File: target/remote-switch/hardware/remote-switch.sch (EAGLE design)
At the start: 89 parts, among them IC1 MEGA8-P, IC2 LTC485N, Q2 BSS123, T1 TIC225S, T2 TIC225S, T3 TIC225S, T4 TIC225S

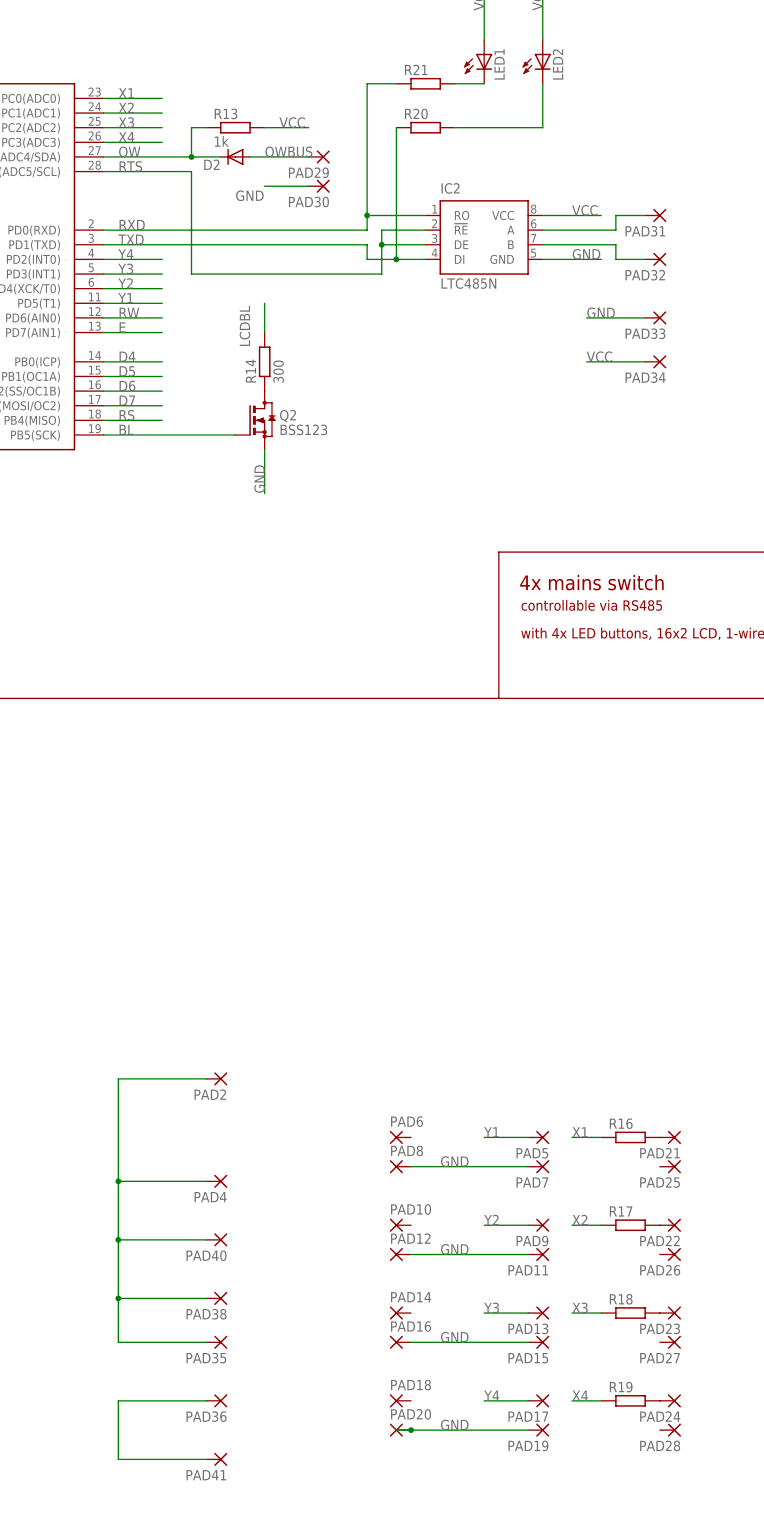
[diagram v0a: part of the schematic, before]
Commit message: remote-switch: firmware - initial revision
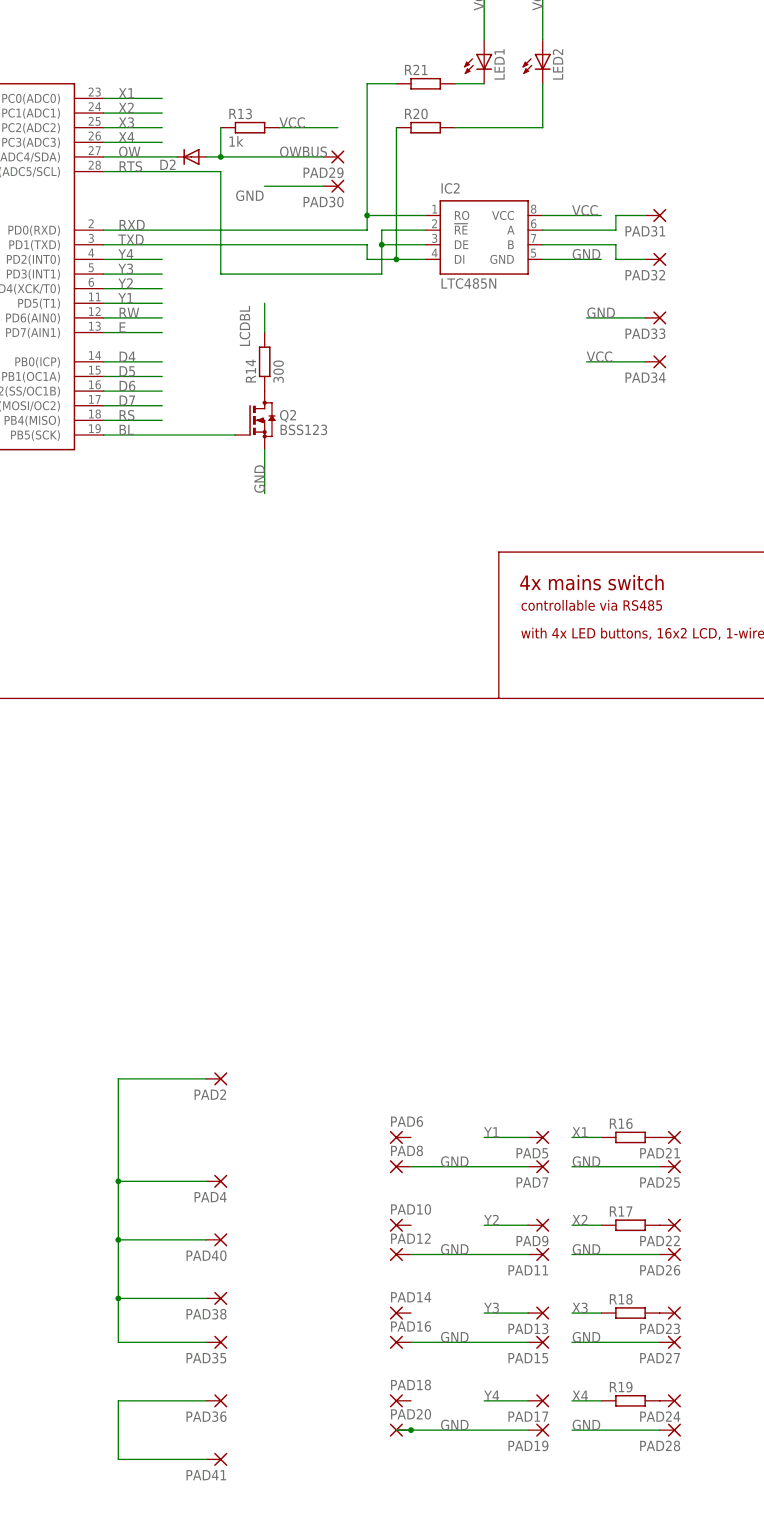
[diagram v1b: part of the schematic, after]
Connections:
- net GND: now also PAD25.P, PAD26.P, PAD27.P, PAD28.P
- net OW: no longer R13.1
- net OWBUS: now also R13.1
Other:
- moved on the sheet: D2, PAD29, PAD30, R13
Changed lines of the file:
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@@
 <instance part="IC1" gate="G$1" x="109.22" y="76.2"/>
 <instance part="Q1" gate="G$1" x="68.58" y="83.82" rot="R90"/>
-<instance part="R13" gate="G$1" x="157.48" y="99.06"/>
-<instance part="D2" gate="G$1" x="157.48" y="93.98" rot="R180"/>
-<instance part="PAD29" gate="P" x="172.72" y="93.98" rot="R180"/>
-<instance part="PAD30" gate="P" x="172.72" y="88.9" rot="R180"/>
+<instance part="R13" gate="G$1" x="160.02" y="99.06"/>
+<instance part="D2" gate="G$1" x="149.86" y="93.98" rot="R180"/>
+<instance part="PAD29" gate="P" x="175.26" y="93.98" rot="R180"/>
+<instance part="PAD30" gate="P" x="175.26" y="88.9" rot="R180"/>
 <instance part="Q2" gate="G$1" x="162.56" y="48.26"/>
 <instance part="R14" gate="G$1" x="162.56" y="58.42" rot="R90"/>
@@
 <segment>
 <pinref part="PAD30" gate="P" pin="P"/>
-<wire x1="170.18" y1="88.9" x2="162.56" y2="88.9" width="0.1524" layer="91"/>
+<wire x1="172.72" y1="88.9" x2="162.56" y2="88.9" width="0.1524" layer="91"/>
 <label x="157.48" y="86.36" size="1.778" layer="95"/>
 </segment>
@@
 <wire x1="152.4" y1="147.32" x2="139.7" y2="147.32" width="0.1524" layer="91"/>
 <label x="144.78" y="147.32" size="1.778" layer="95" rot="R180"/>
+</segment>
+<segment>
+<pinref part="PAD25" gate="P" pin="P"/>
+<wire x1="231.14" y1="-81.28" x2="215.9" y2="-81.28" width="0.1524" layer="91"/>
+<label x="215.9" y="-81.28" size="1.778" layer="95"/>
+</segment>
+<segment>
+<pinref part="PAD26" gate="P" pin="P"/>
+<wire x1="231.14" y1="-96.52" x2="215.9" y2="-96.52" width="0.1524" layer="91"/>
+<label x="215.9" y="-96.52" size="1.778" layer="95"/>
+</segment>
+<segment>
+<pinref part="PAD27" gate="P" pin="P"/>
+<wire x1="231.14" y1="-111.76" x2="215.9" y2="-111.76" width="0.1524" layer="91"/>
+<label x="215.9" y="-111.76" size="1.778" layer="95"/>
+</segment>
+<segment>
+<pinref part="PAD28" gate="P" pin="P"/>
+<wire x1="231.14" y1="-127" x2="215.9" y2="-127" width="0.1524" layer="91"/>
+<label x="215.9" y="-127" size="1.778" layer="95"/>
 </segment>
 </net>
@@
 <segment>
 <pinref part="IC1" gate="G$1" pin="PC4(ADC4/SDA)"/>
-<wire x1="134.62" y1="93.98" x2="149.86" y2="93.98" width="0.1524" layer="91"/>
+<wire x1="134.62" y1="93.98" x2="147.32" y2="93.98" width="0.1524" layer="91"/>
 <label x="137.16" y="93.98" size="1.778" layer="95"/>
-<pinref part="R13" gate="G$1" pin="1"/>
-<wire x1="149.86" y1="93.98" x2="154.94" y2="93.98" width="0.1524" layer="91"/>
-<wire x1="152.4" y1="99.06" x2="149.86" y2="99.06" width="0.1524" layer="91"/>
-<wire x1="149.86" y1="99.06" x2="149.86" y2="93.98" width="0.1524" layer="91"/>
-<junction x="149.86" y="93.98"/>
 <pinref part="D2" gate="G$1" pin="C"/>
 </segment>
@@
 <segment>
 <pinref part="IC1" gate="G$1" pin="PC5(ADC5/SCL)"/>
-<wire x1="134.62" y1="91.44" x2="149.86" y2="91.44" width="0.1524" layer="91"/>
+<wire x1="134.62" y1="91.44" x2="154.94" y2="91.44" width="0.1524" layer="91"/>
 <label x="137.16" y="91.44" size="1.778" layer="95"/>
-<wire x1="149.86" y1="91.44" x2="149.86" y2="73.66" width="0.1524" layer="91"/>
-<wire x1="149.86" y1="73.66" x2="182.88" y2="73.66" width="0.1524" layer="91"/>
+<wire x1="154.94" y1="91.44" x2="154.94" y2="73.66" width="0.1524" layer="91"/>
+<wire x1="154.94" y1="73.66" x2="182.88" y2="73.66" width="0.1524" layer="91"/>
 <pinref part="IC2" gate="G$1" pin="!RE"/>
 <wire x1="190.5" y1="81.28" x2="182.88" y2="81.28" width="0.1524" layer="91"/>
@@
 <segment>
 <pinref part="R13" gate="G$1" pin="2"/>
-<wire x1="162.56" y1="99.06" x2="170.18" y2="99.06" width="0.1524" layer="91"/>
+<wire x1="165.1" y1="99.06" x2="175.26" y2="99.06" width="0.1524" layer="91"/>
 <label x="165.1" y="99.06" size="1.778" layer="95"/>
 </segment>
@@
 <net name="OWBUS" class="0">
 <segment>
-<wire x1="160.02" y1="93.98" x2="170.18" y2="93.98" width="0.1524" layer="91"/>
-<label x="162.56" y="93.98" size="1.778" layer="95"/>
+<wire x1="152.4" y1="93.98" x2="154.94" y2="93.98" width="0.1524" layer="91"/>
+<label x="165.1" y="93.98" size="1.778" layer="95"/>
 <pinref part="D2" gate="G$1" pin="A"/>
 <pinref part="PAD29" gate="P" pin="P"/>
-</segment>
-</net>
+<pinref part="R13" gate="G$1" pin="1"/>
+<wire x1="154.94" y1="93.98" x2="172.72" y2="93.98" width="0.1524" layer="91"/>
+<wire x1="154.94" y1="99.06" x2="154.94" y2="93.98" width="0.1524" layer="91"/>
+<junction x="154.94" y="93.98"/>
+</segment>
+</net>
